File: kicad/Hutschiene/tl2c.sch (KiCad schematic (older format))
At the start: 29 parts, among them IC101 ATTINY20-X, P101 12VDC, P102 RJ45, P103 CTL CONN, P104 TPI Header, P105 DRV CONN, P106 240VAC, P108 UG, P109 5VDC, P110 EG, P111 OG, SW101 TL3315NF160Q

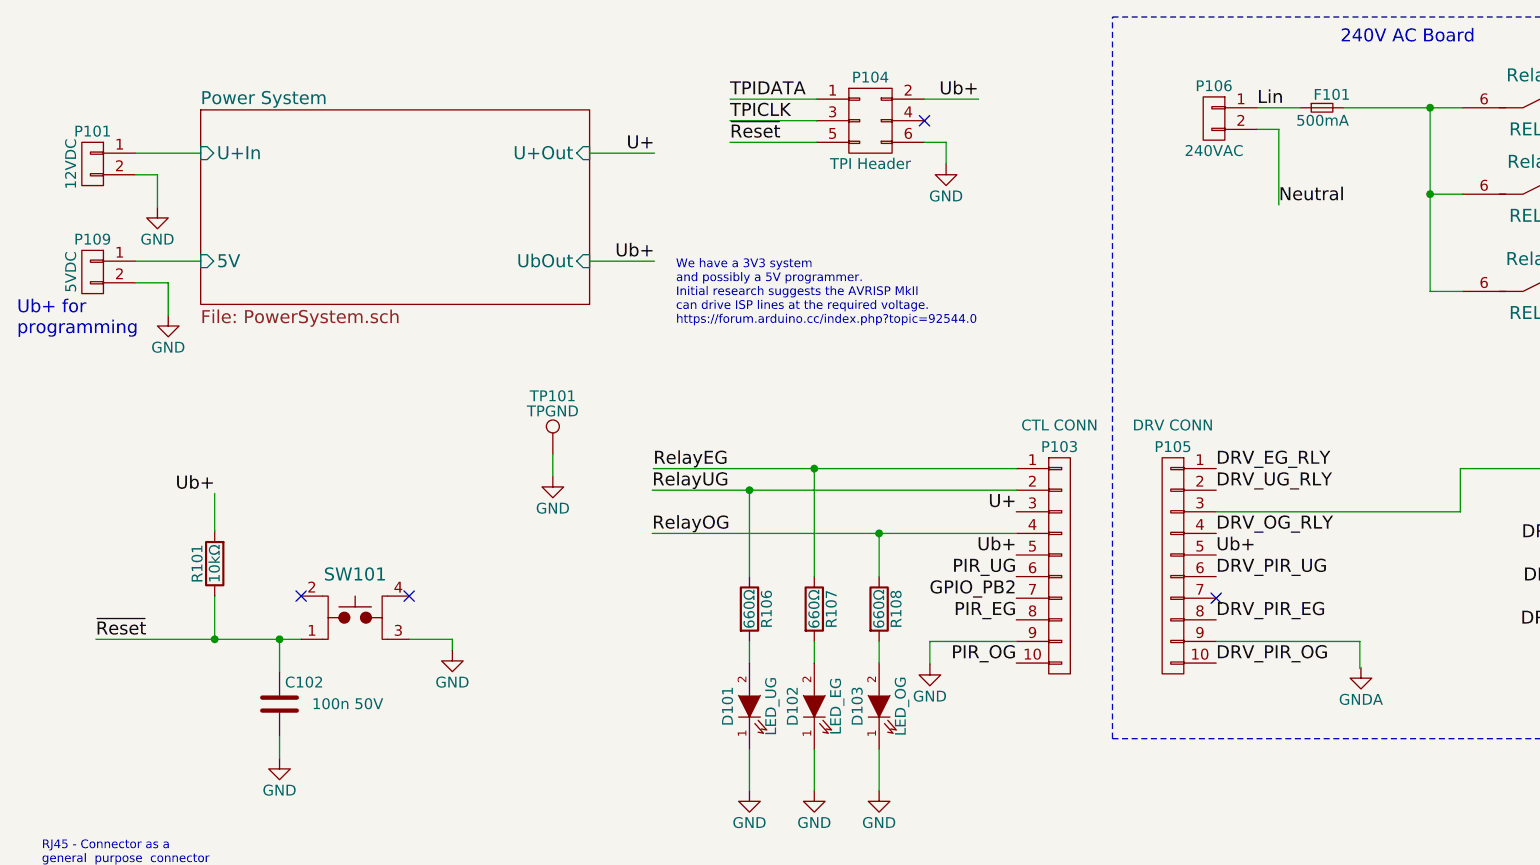
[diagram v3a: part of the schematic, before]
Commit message: Further to the layout for the Hutschiene
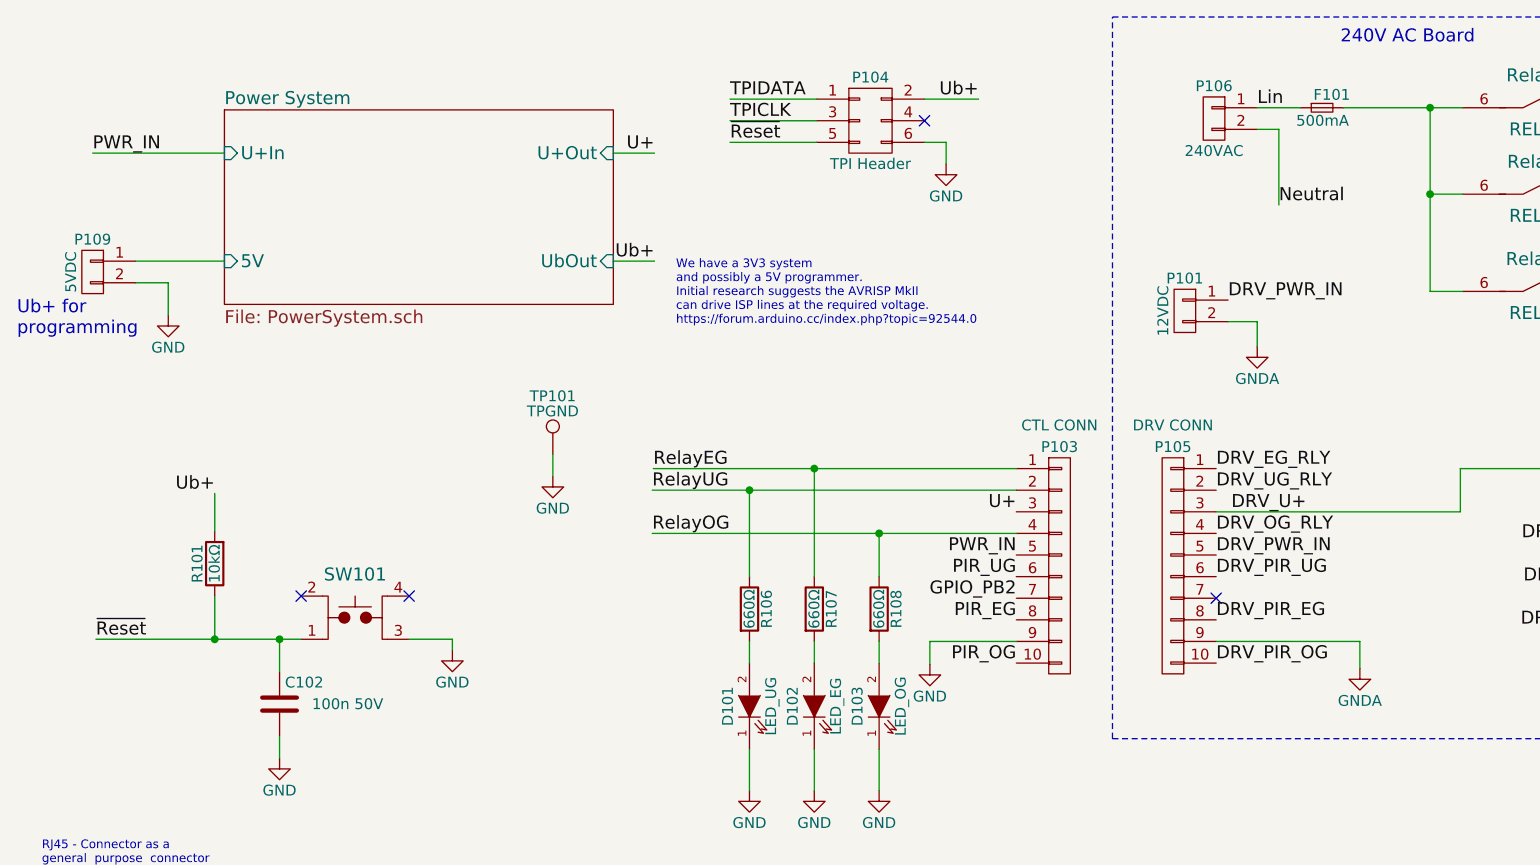
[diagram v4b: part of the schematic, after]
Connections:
- net GND: no longer P101.2 (P2)
- net GNDA: now also P101.2 (P2), P105.9 (P9)
- net Ub+: no longer P103.5 (P5), P105.5 (P5)
- net LED Driver/LED_DRIVER_U+ renamed DRV_U+
- net Power System/U+In renamed DRV_PWR_IN
- net DRV_PWR_IN: now also P105.5 (P5)
- new net PWR_IN: P103.5 (P5)
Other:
- moved on the sheet: P101
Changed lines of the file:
@@
 TODO - Verify the values \nof the resistors for sharing\nthe IO lines.
 $Sheet
-S 1400 1150 1800 900
+S 1510 1150 1800 900
 U 584D9013
 F0 "Power System" 60
 F1 "PowerSystem.sch" 60
-F2 "UbOut" I R 3200 1850 60
-F3 "U+Out" I R 3200 1350 60
-F4 "U+In" I L 1400 1350 60
-F5 "5V" I L 1400 1850 60
+F2 "UbOut" I R 3310 1850 60
+F3 "U+Out" I R 3310 1350 60
+F4 "U+In" I L 1510 1350 60
+F5 "5V" I L 1510 1850 60
 $EndSheet
 $Comp
 L CONN_01X02 P101
 U 1 1 584D9CD6
-P 900 1400
-F 0 "P101" H 900 1550 50  0000 C CNN
-F 1 "12VDC" V 1000 1400 50  0000 C CNN
-F 2 "tl2c-footprint:PCB_Screw_Terminal_Block_5mm_x_2" H 900 1400 50  0001 C CNN
-F 3 "" H 900 1400 50  0000 C CNN
-F 4 "Value" H 900 1400 60  0001 C CNN "MFP"
-F 5 "Value" H 900 1400 60  0001 C CNN "Conrad-PN"
-F 6 "Value" H 900 1400 60  0001 C CNN "Digikey-PN"
-	1    900  1400
+P 5955 2080
+F 0 "P101" H 5955 2230 50  0000 C CNN
+F 1 "12VDC" V 6055 2080 50  0000 C CNN
+F 2 "tl2c-footprint:PCB_Screw_Terminal_Block_5mm_x_2" H 5955 2080 50  0001 C CNN
+F 3 "" H 5955 2080 50  0000 C CNN
+F 4 "Value" H 5955 2080 60  0001 C CNN "MFP"
+F 5 "Value" H 5955 2080 60  0001 C CNN "Conrad-PN"
+F 6 "Value" H 5955 2080 60  0001 C CNN "Digikey-PN"
+	1    5955 2080
 	-1   0    0    -1
 $EndComp
@@
 Text Label 3500 1850 2    60   ~ 0
 Ub+
-$Comp
-L GND #PWR06
-U 1 1 584DF6BA
-P 1200 1600
-F 0 "#PWR06" H 1200 1350 50  0001 C CNN
-F 1 "GND" H 1200 1450 50  0000 C CNN
-F 2 "" H 1200 1600 50  0000 C CNN
-F 3 "" H 1200 1600 50  0000 C CNN
-	1    1200 1600
-	1    0    0    -1
-$EndComp
 $Comp
 L TEST_1P TP101
@@
 $EndComp
 $Comp
-L GND #PWR07
+L GND #PWR06
 U 1 1 584E33BE
 P 3030 2845
-F 0 "#PWR07" H 3030 2595 50  0001 C CNN
+F 0 "#PWR06" H 3030 2595 50  0001 C CNN
 F 1 "GND" H 3030 2695 50  0000 C CNN
 F 2 "" H 3030 2845 50  0000 C CNN
@@
 $EndComp
 $Comp
-L GND #PWR08
+L GND #PWR07
 U 1 1 5856AF1B
 P 3940 4300
-F 0 "#PWR08" H 3940 4050 50  0001 C CNN
+F 0 "#PWR07" H 3940 4050 50  0001 C CNN
 F 1 "GND" H 3940 4150 50  0000 C CNN
 F 2 "" H 3940 4300 50  0000 C CNN
@@
 $EndComp
 $Comp
-L GND #PWR09
+L GND #PWR08
 U 1 1 5856B284
 P 4240 4300
-F 0 "#PWR09" H 4240 4050 50  0001 C CNN
+F 0 "#PWR08" H 4240 4050 50  0001 C CNN
 F 1 "GND" H 4240 4150 50  0000 C CNN
 F 2 "" H 4240 4300 50  0000 C CNN
@@
 $EndComp
 $Comp
-L GND #PWR010
+L GND #PWR09
 U 1 1 5856B510
 P 4540 4300
-F 0 "#PWR010" H 4540 4050 50  0001 C CNN
+F 0 "#PWR09" H 4540 4050 50  0001 C CNN
 F 1 "GND" H 4540 4150 50  0000 C CNN
 F 2 "" H 4540 4300 50  0000 C CNN
@@
 $EndComp
 $Comp
-L GNDA #PWR011
+L GNDA #PWR010
 U 1 1 5856E00B
-P 6770 3730
-F 0 "#PWR011" H 6770 3480 50  0001 C CNN
-F 1 "GNDA" H 6770 3580 50  0000 C CNN
-F 2 "" H 6770 3730 50  0000 C CNN
-F 3 "" H 6770 3730 50  0000 C CNN
-	1    6770 3730
+P 6765 3735
+F 0 "#PWR010" H 6765 3485 50  0001 C CNN
+F 1 "GNDA" H 6765 3585 50  0000 C CNN
+F 2 "" H 6765 3735 50  0000 C CNN
+F 3 "" H 6765 3735 50  0000 C CNN
+	1    6765 3735
 	-1   0    0    -1
 $EndComp
@@
 $EndComp
 $Comp
-L GND #PWR012
+L GND #PWR011
 U 1 1 5867873E
 P 1765 4150
-F 0 "#PWR012" H 1765 3900 50  0001 C CNN
+F 0 "#PWR011" H 1765 3900 50  0001 C CNN
 F 1 "GND" H 1765 4000 50  0000 C CNN
 F 2 "" H 1765 4150 50  0000 C CNN
@@
 	1    0    0    -1
 $EndComp
-Text Label 5175 3210 2    60   ~ 0
-Ub+
 Text Label 5175 3410 2    60   ~ 0
 GPIO_PB2
@@
 $EndComp
 $Comp
-L GND #PWR013
+L GND #PWR012
 U 1 1 589A5184
 P 1250 2100
-F 0 "#PWR013" H 1250 1850 50  0001 C CNN
+F 0 "#PWR012" H 1250 1850 50  0001 C CNN
 F 1 "GND" H 1250 1950 50  0000 C CNN
 F 2 "" H 1250 2100 50  0000 C CNN
@@
 $EndComp
 $Comp
-L GND #PWR014
+L GND #PWR013
 U 1 1 596B9253
 P 1615 5810
-F 0 "#PWR014" H 1615 5560 50  0001 C CNN
+F 0 "#PWR013" H 1615 5560 50  0001 C CNN
 F 1 "GND" H 1615 5660 50  0000 C CNN
 F 2 "" H 1615 5810 50  0000 C CNN
@@
 	2565 3600 2565 3650
 Wire Wire Line
-	1100 1350 1400 1350
-Wire Wire Line
-	3200 1350 3500 1350
-Wire Wire Line
-	3200 1850 3500 1850
-Wire Wire Line
-	1100 1450 1200 1450
-Wire Wire Line
-	1200 1450 1200 1600
+	900  1350 1510 1350
+Wire Wire Line
+	3310 1350 3500 1350
+Wire Wire Line
+	3310 1850 3500 1850
 Wire Wire Line
 	7760 5020 7360 5020
@@
 	4710 6820 5110 6820
 Wire Wire Line
-	1100 1850 1400 1850
+	1100 1850 1510 1850
 Wire Wire Line
 	1100 1950 1250 1950
@@
 DRV_PIR_UG
 $Comp
-L GNDA #PWR015
+L GNDA #PWR014
 U 1 1 596D914D
 P 7770 3810
-F 0 "#PWR015" H 7770 3560 50  0001 C CNN
+F 0 "#PWR014" H 7770 3560 50  0001 C CNN
 F 1 "GNDA" H 7770 3660 50  0000 C CNN
 F 2 "" H 7770 3810 50  0000 C CNN
@@
 $EndComp
 $Comp
-L GND #PWR016
+L GND #PWR015
 U 1 1 596DB6E6
 P 4775 3715
-F 0 "#PWR016" H 4775 3465 50  0001 C CNN
+F 0 "#PWR015" H 4775 3465 50  0001 C CNN
 F 1 "GND" H 4775 3565 50  0000 C CNN
 F 2 "" H 4775 3715 50  0000 C CNN
@@
 $EndComp
 Text Label 6100 3210 0    60   ~ 0
-Ub+
+DRV_PWR_IN
 NoConn ~ 6100 3410
 Wire Wire Line
@@
 	7230 3010 6100 3010
 Connection ~ 7620 2810
+$Comp
+L GNDA #PWR016
+U 1 1 596F996D
+P 6290 2245
+F 0 "#PWR016" H 6290 1995 50  0001 C CNN
+F 1 "GNDA" H 6290 2095 50  0000 C CNN
+F 2 "" H 6290 2245 50  0000 C CNN
+F 3 "" H 6290 2245 50  0000 C CNN
+	1    6290 2245
+	-1   0    0    -1
+$EndComp
+Text Label 6170 3010 0    60   ~ 0
+DRV_U+
+Text Label 5175 3210 2    60   ~ 0
+PWR_IN
+Text Label 900  1350 0    60   ~ 0
+PWR_IN
+Text Label 6155 2030 0    60   ~ 0
+DRV_PWR_IN
+Wire Wire Line
+	6155 2130 6290 2130
+Wire Wire Line
+	6290 2130 6290 2245
 $EndSCHEMATC

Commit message: Hutschiene layout intermediate save
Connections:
- net DRV_OG_RLY: now also P105.5 (P5); no longer P105.4 (P4)
- net DRV_PWR_IN: now also P105.4 (P4); no longer P105.5 (P5)
- net PWR_IN: now also P103.4 (P4); no longer P103.5 (P5)
- net RelayOG: now also P103.5 (P5); no longer P103.4 (P4)

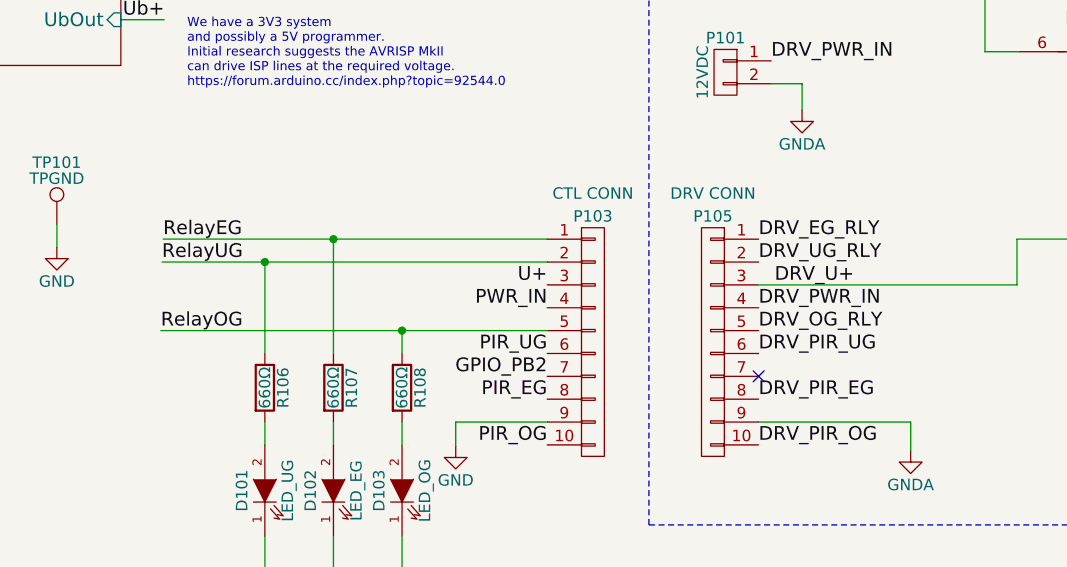
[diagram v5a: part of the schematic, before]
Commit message: Completed draft of hutshiene layout
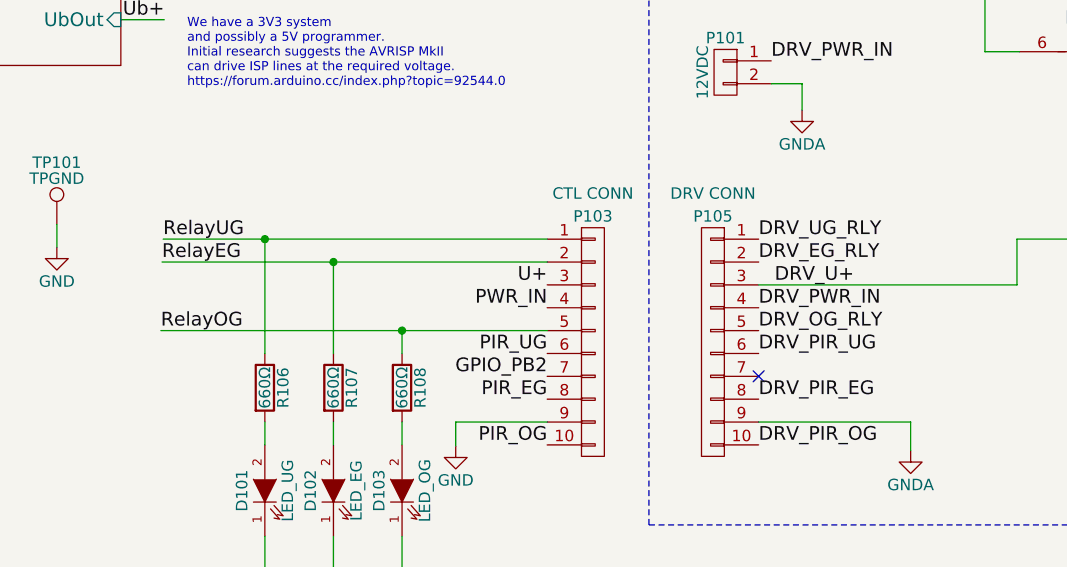
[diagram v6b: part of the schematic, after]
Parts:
- P102: footprint Connect:RJ45_8 -> tl2c-footprint:RJ45_8P8C
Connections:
- net DRV_EG_RLY: now also P105.2 (P2); no longer P105.1 (P1)
- net DRV_UG_RLY: now also P105.1 (P1); no longer P105.2 (P2)
- net RelayEG: now also P103.2 (P2); no longer P103.1 (P1)
- net RelayUG: now also P103.1 (P1); no longer P103.2 (P2)
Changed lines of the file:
@@
 F6 "LED_DRIVER_GND" I L 8050 3670 60
 $EndSheet
+Text Label 3495 2810 0    60   ~ 0
+RelayUG
 Text Label 3490 2910 0    60   ~ 0
-RelayUG
-Text Label 3495 2810 0    60   ~ 0
 RelayEG
 Text Label 3485 3210 0    60   ~ 0
@@
 F 0 "P102" H 715 5710 50  0000 C CNN
 F 1 "RJ45" V 815 5260 50  0000 C CNN
-F 2 "Connect:RJ45_8" H 715 5260 50  0001 C CNN
+F 2 "tl2c-footprint:RJ45_8P8C" H 715 5260 50  0001 C CNN
 F 3 "" H 715 5260 50  0000 C CNN
 	1    715  5260
@@
 	-1   0    0    -1
 $EndComp
-Text Label 6100 2910 0    60   ~ 0
+Text Label 6100 2810 0    60   ~ 0
 DRV_UG_RLY
 Text Label 8050 3150 2    60   ~ 0
 DRV_UG_RLY
-Text Label 6100 2810 0    60   ~ 0
+Text Label 6100 2910 0    60   ~ 0
 DRV_EG_RLY
 Text Label 6100 3210 0    60   ~ 0
@@
 	4710 6120 5360 6120
 Wire Wire Line
-	3940 3310 3940 2910
-Wire Wire Line
-	4240 2810 4240 3310
-Wire Wire Line
 	915  3600 1865 3600
 Wire Wire Line
@@
 Wire Wire Line
 	6765 3610 6100 3610
-Connection ~ 3940 2910
 Wire Wire Line
 	3490 2910 5175 2910
 Wire Wire Line
 	3495 2810 5175 2810
-Connection ~ 4240 2810
 Wire Wire Line
 	7230 2810 7230 3010
@@
 	4540 3310 4540 3210
 Connection ~ 4540 3210
+Wire Wire Line
+	4240 3310 4240 2910
+Connection ~ 4240 2910
+Wire Wire Line
+	3940 3310 3940 2810
+Connection ~ 3940 2810
 $EndSCHEMATC

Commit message: Adjusted the size and location of the terminal blocks
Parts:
- P101, P106, P108, P110, P111: footprint tl2c-footprint:PCB_Screw_Terminal_Block_5mm_x_2 -> tl2c-footprint:PCB_Screw_Terminal_Block_5.08mm_x_2
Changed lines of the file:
@@
 F 0 "P101" H 5955 2230 50  0000 C CNN
 F 1 "12VDC" V 6055 2080 50  0000 C CNN
-F 2 "tl2c-footprint:PCB_Screw_Terminal_Block_5mm_x_2" H 5955 2080 50  0001 C CNN
+F 2 "tl2c-footprint:PCB_Screw_Terminal_Block_5.08mm_x_2" H 5955 2080 50  0001 C CNN
 F 3 "" H 5955 2080 50  0000 C CNN
 F 4 "Value" H 5955 2080 60  0001 C CNN "MFP"
@@
 F 0 "P108" H 9560 1225 50  0000 C CNN
 F 1 "UG" H 9490 1125 50  0000 C CNN
-F 2 "tl2c-footprint:PCB_Screw_Terminal_Block_5mm_x_2" H 9390 1190 50  0001 C CNN
+F 2 "tl2c-footprint:PCB_Screw_Terminal_Block_5.08mm_x_2" H 9390 1190 50  0001 C CNN
 F 3 "" H 9390 1190 50  0000 C CNN
 F 4 "Value" H 9390 1190 60  0001 C CNN "MFP"
@@
 F 0 "P110" H 9555 1430 50  0000 C CNN
 F 1 "EG" H 9490 1345 50  0000 C CNN
-F 2 "tl2c-footprint:PCB_Screw_Terminal_Block_5mm_x_2" H 9390 1390 50  0001 C CNN
+F 2 "tl2c-footprint:PCB_Screw_Terminal_Block_5.08mm_x_2" H 9390 1390 50  0001 C CNN
 F 3 "" H 9390 1390 50  0000 C CNN
 F 4 "Value" H 9390 1390 60  0001 C CNN "MFP"
@@
 F 0 "P111" H 9545 1635 50  0000 C CNN
 F 1 "OG" H 9505 1535 50  0000 C CNN
-F 2 "tl2c-footprint:PCB_Screw_Terminal_Block_5mm_x_2" H 9390 1590 50  0001 C CNN
+F 2 "tl2c-footprint:PCB_Screw_Terminal_Block_5.08mm_x_2" H 9390 1590 50  0001 C CNN
 F 3 "" H 9390 1590 50  0000 C CNN
 F 4 "Value" H 9390 1590 60  0001 C CNN "MFP"
@@
 F 0 "P106" H 6090 1340 50  0000 C CNN
 F 1 "240VAC" H 6090 1040 50  0000 C CNN
-F 2 "tl2c-footprint:PCB_Screw_Terminal_Block_5mm_x_2" H 6090 1190 50  0001 C CNN
+F 2 "tl2c-footprint:PCB_Screw_Terminal_Block_5.08mm_x_2" H 6090 1190 50  0001 C CNN
 F 3 "" H 6090 1190 50  0000 C CNN
 F 4 "Value" H 6090 1190 60  0001 C CNN "MFP"
